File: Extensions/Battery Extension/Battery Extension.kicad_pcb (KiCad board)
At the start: 2 copper layers, 49.1 x 18.7 mm, 23 parts, among them P4 Solder_Pad, U1 M1250RS-02P, U10 WJ126V-5_0-3P, U11 WJ126V-5_0-3P, U3 FS8205A, U4 TPS61032PWPR, U5 TP4056, U6 DW01A, U7 FXL0530-6R8-M, U8 AP40P05

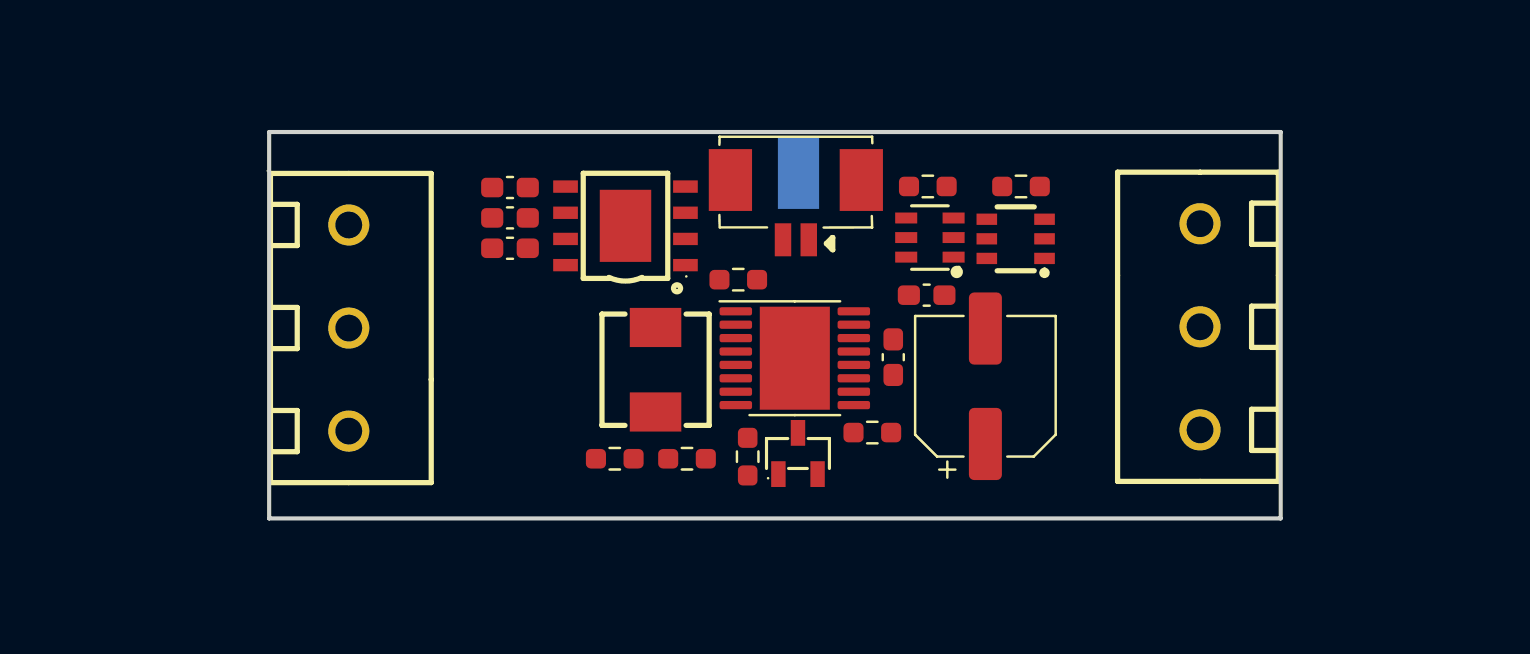
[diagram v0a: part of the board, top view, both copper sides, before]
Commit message: started replacing 0603 with 0402 caps and resistor
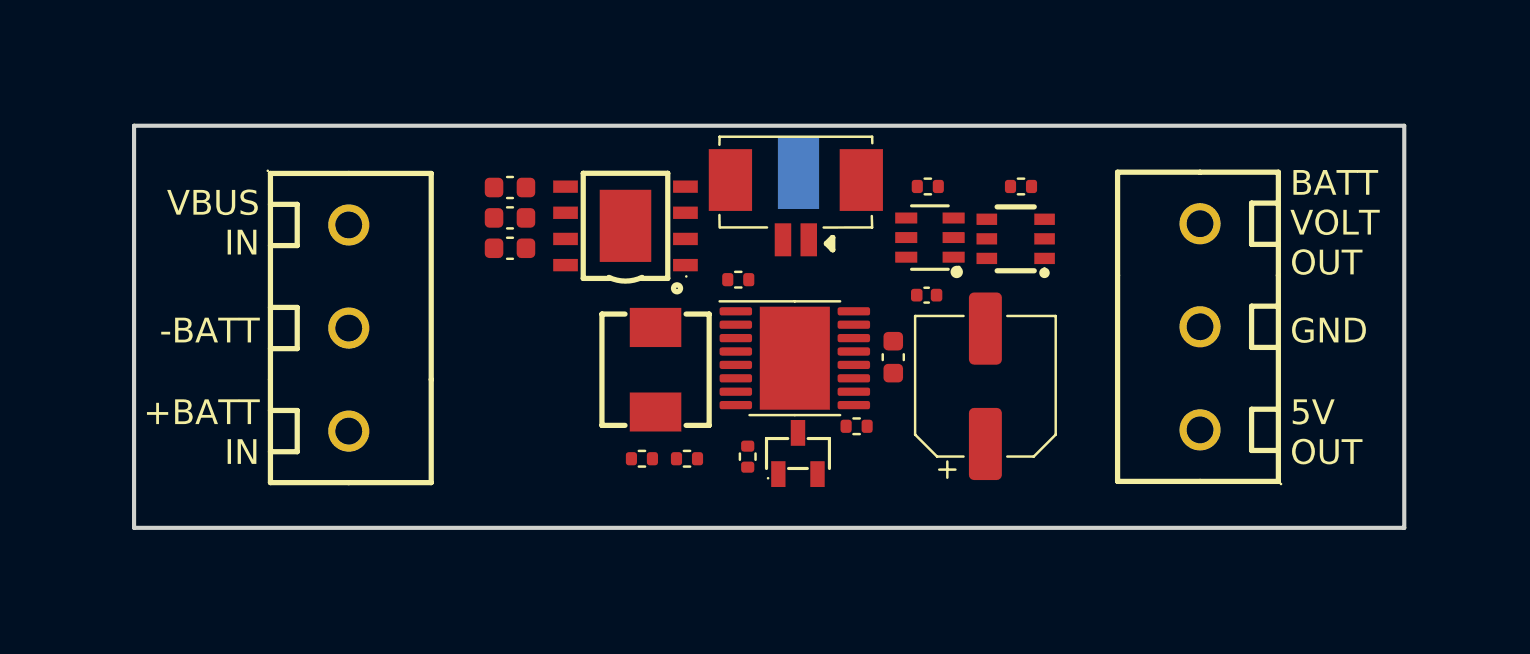
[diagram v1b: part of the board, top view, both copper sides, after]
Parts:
- C1, C2, C3, C4: footprint Capacitor_SMD:C_0603_1608Metric_Pad1.08x0.95mm_HandSolder -> Capacitor_SMD:C_0603_1608Metric
- C5: footprint Capacitor_SMD:C_0603_1608Metric_Pad1.08x0.95mm_HandSolder -> Capacitor_SMD:C_0402_1005Metric
- R1, R2, R5, R6, R8, R9: footprint Resistor_SMD:R_0603_1608Metric_Pad0.98x0.95mm_HandSolder -> Resistor_SMD:R_0402_1005Metric
- R7: value 5.1K -> 2K; footprint Resistor_SMD:R_0603_1608Metric_Pad0.98x0.95mm_HandSolder -> Resistor_SMD:R_0402_1005Metric
- moved R2 1.32 mm to (53.4, 59.0)
- moved R9 0.82 mm to (63.8, 57.5)
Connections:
- net IO27/BATT CHARGING renamed BATT CHARGING
- R1 pad 1: IO26/BATT VOLT -> BATT VOLT
- R2 pad 2: IO26/BATT VOLT -> BATT VOLT
- U10 pad 1: IO26/BATT VOLT -> VBUS
- U11 pad 3: VBUS -> BATT VOLT
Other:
- board size 49.1 x 18.7 mm -> 61.6 x 19.5 mm
- board text added: "+BATT IN"
- board text added: "-BATT"
- board text added: "5V OUT"
- board text added: "BATT VOLT OUT"
- board text added: "GND"
- board text added: "VBUS IN"

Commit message: updated GlowCore PCB
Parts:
- R1: value 100K -> 33K
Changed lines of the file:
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@@
     (descr "Resistor SMD 0402 (1005 Metric), square (rectangular) end terminal, IPC_7351 nominal, (Body size source: IPC-SM-782 page 72, https://www.pcb-3d.com/wordpress/wp-content/uploads/ipc-sm-782a_amendment_1_and_2.pdf), generated with kicad-footprint-generator")
     (tags "resistor")
-    (property "LCSC #" "C25741")
+    (property "LCSC #" "C25779")
     (property "Sheetfile" "Battery Extension.kicad_sch")
     (property "Sheetname" "")
@@
       (effects (font (size 1 1) (thickness 0.15)))
     )
-    (fp_text value "100K" (at 0 1.17) (layer "F.Fab")
+    (fp_text value "33K" (at 0 1.17) (layer "F.Fab")
       (effects (font (size 1 1) (thickness 0.15)))
     )
